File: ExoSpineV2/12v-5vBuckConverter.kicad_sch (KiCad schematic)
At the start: 14 parts, among them J19 Screw_Terminal_01x02, U5 TPS564247

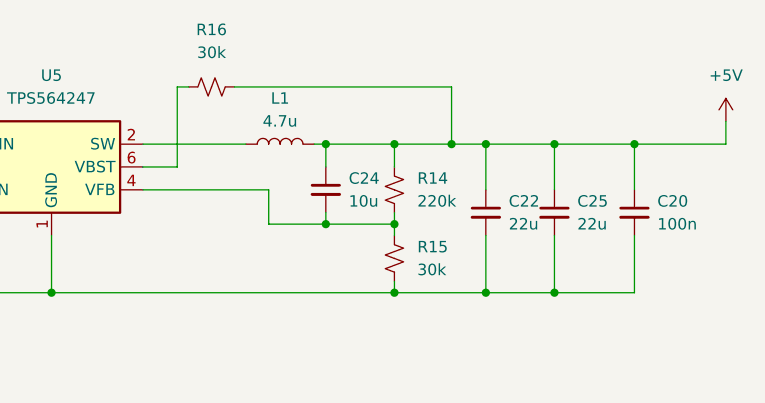
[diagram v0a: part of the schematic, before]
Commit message: dimensionnement des composantes pour le DC-DC
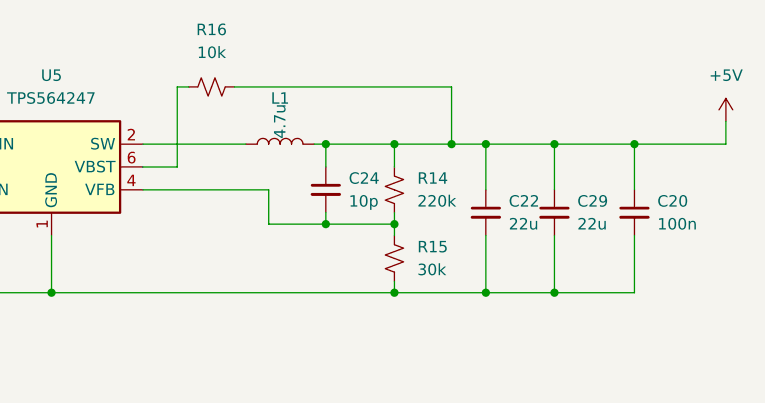
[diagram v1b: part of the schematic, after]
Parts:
- removed C25: 22u, symbol Device:C_Small
- added C29: 22u, Capacitor_SMD:C_0805_2012Metric_Pad1.18x1.45mm_HandSolder, symbol Device:C_Small
- C20, C21, C23: footprint (none) -> Capacitor_SMD:C_1206_3216Metric_Pad1.33x1.80mm_HandSolder
- C22: footprint (none) -> Capacitor_SMD:C_0805_2012Metric_Pad1.18x1.45mm_HandSolder
- C24: value 10u -> 10p; footprint (none) -> Capacitor_SMD:C_0201_0603Metric_Pad0.64x0.40mm_HandSolder
- L1: footprint (none) -> Inductor_SMD:L_Bourns_SRP7028A_7.3x6.6mm
- R12, R13, R14, R15: footprint (none) -> Resistor_SMD:R_0805_2012Metric_Pad1.20x1.40mm_HandSolder
- R16: value 30k -> 10k; footprint (none) -> Resistor_SMD:R_0805_2012Metric_Pad1.20x1.40mm_HandSolder
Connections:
- net +5V: now also R16.1, C29.1; no longer R16.2
- net GND: now also R15.1, C29.2; no longer R15.2
- net at U5.6 (VBST): now also R16.2; no longer R16.1
- net at C24.2, R14.2, U5.4 (VFB): now also R15.2; no longer R15.1

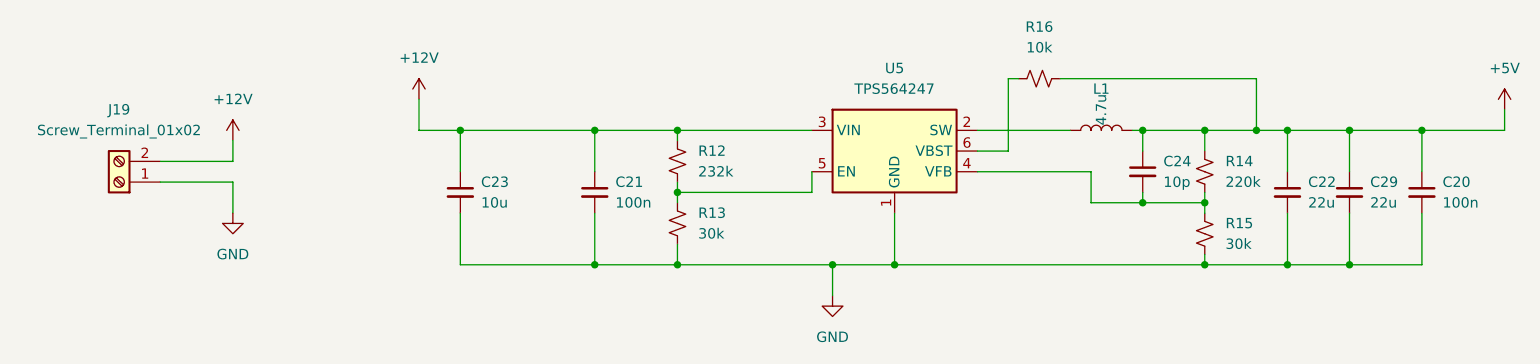
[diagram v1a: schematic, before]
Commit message: ajout de composantes au board
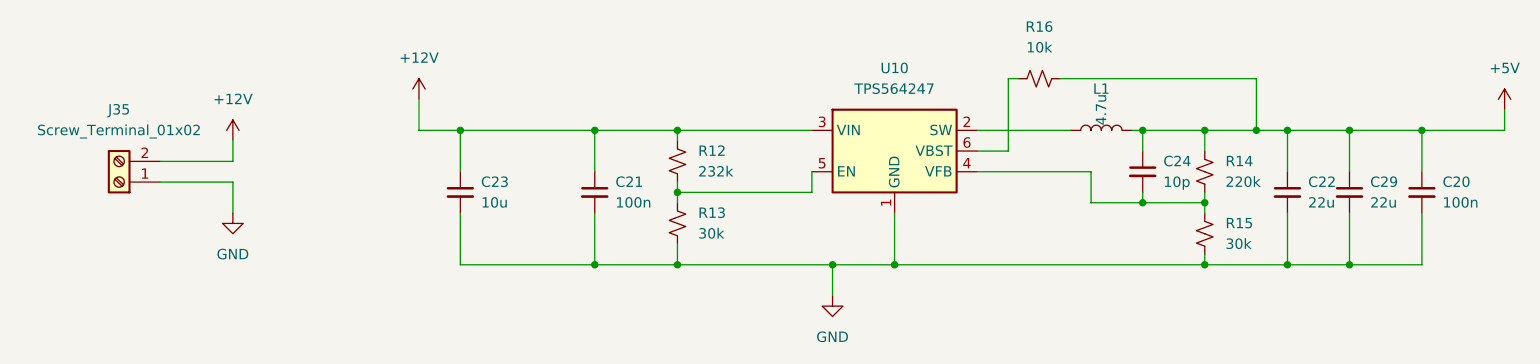
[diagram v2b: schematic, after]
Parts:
- renumbered J19 to J35, U5 to U10
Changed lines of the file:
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@@
   (symbol (lib_id "Connector:Screw_Terminal_01x02") (at 46.99 85.09 180) (unit 1)
     (in_bom yes) (on_board yes) (dnp no) (fields_autoplaced)
-    (property "Reference" "J19" (at 46.99 76.2 0)
+    (property "Reference" "J35" (at 46.99 76.2 0)
       (effects (font (size 1.27 1.27)))
     )
@@
       (project "ExospineV2"
         (path "/e63e39d7-6ac0-4ffd-8aa3-1841a4541b55/9042656c-fbb6-4ad3-be09-ad4e06445cda"
-          (reference "J19") (unit 1)
+          (reference "J35") (unit 1)
         )
       )
@@
   (symbol (lib_id "power:+12V") (at 83.82 74.93 0) (unit 1)
     (in_bom yes) (on_board yes) (dnp no) (fields_autoplaced)
-    (property "Reference" "#PWR011" (at 83.82 78.74 0)
+    (property "Reference" "#PWR0101" (at 83.82 78.74 0)
       (effects (font (size 1.27 1.27)) hide)
     )
@@
       (project "ExospineV2"
         (path "/e63e39d7-6ac0-4ffd-8aa3-1841a4541b55/9042656c-fbb6-4ad3-be09-ad4e06445cda"
-          (reference "#PWR011") (unit 1)
+          (reference "#PWR0101") (unit 1)
         )
       )
@@
   (symbol (lib_id "Regulator_Switching:TPS563200") (at 142.24 81.28 0) (unit 1)
     (in_bom yes) (on_board yes) (dnp no) (fields_autoplaced)
-    (property "Reference" "U5" (at 142.24 71.12 0)
+    (property "Reference" "U10" (at 142.24 71.12 0)
       (effects (font (size 1.27 1.27)))
     )
@@
       (project "ExospineV2"
         (path "/e63e39d7-6ac0-4ffd-8aa3-1841a4541b55/9042656c-fbb6-4ad3-be09-ad4e06445cda"
-          (reference "U5") (unit 1)
+          (reference "U10") (unit 1)
         )
       )
@@
   (symbol (lib_id "power:+5V") (at 217.17 76.2 0) (unit 1)
     (in_bom yes) (on_board yes) (dnp no) (fields_autoplaced)
-    (property "Reference" "#PWR013" (at 217.17 80.01 0)
+    (property "Reference" "#PWR0103" (at 217.17 80.01 0)
       (effects (font (size 1.27 1.27)) hide)
     )
@@
       (project "ExospineV2"
         (path "/e63e39d7-6ac0-4ffd-8aa3-1841a4541b55/9042656c-fbb6-4ad3-be09-ad4e06445cda"
-          (reference "#PWR013") (unit 1)
+          (reference "#PWR0103") (unit 1)
         )
       )
@@
   (symbol (lib_id "power:GND") (at 134.62 99.06 0) (unit 1)
     (in_bom yes) (on_board yes) (dnp no) (fields_autoplaced)
-    (property "Reference" "#PWR014" (at 134.62 105.41 0)
+    (property "Reference" "#PWR0102" (at 134.62 105.41 0)
       (effects (font (size 1.27 1.27)) hide)
     )
@@
       (project "ExospineV2"
         (path "/e63e39d7-6ac0-4ffd-8aa3-1841a4541b55/9042656c-fbb6-4ad3-be09-ad4e06445cda"
-          (reference "#PWR014") (unit 1)
-        )
-      )
+          (reference "#PWR0102") (unit 1)
+        )
+      )

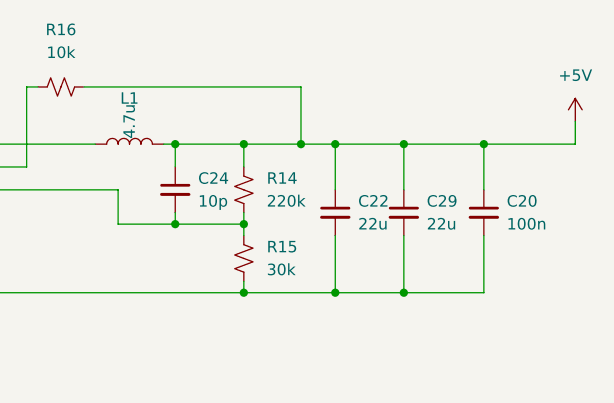
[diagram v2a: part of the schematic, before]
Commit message: dimensionnage de certaines composantes
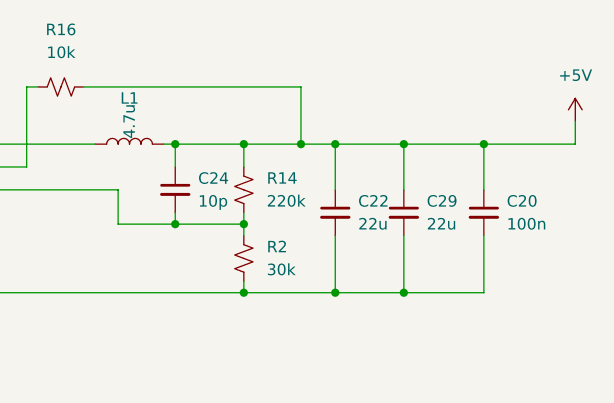
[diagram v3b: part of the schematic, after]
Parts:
- removed R15: 30k, Resistor_SMD:R_0805_2012Metric_Pad1.20x1.40mm_HandSolder, symbol Device:R_Small_US
- added R2: 30k, Resistor_SMD:R_0805_2012Metric_Pad1.20x1.40mm_HandSolder, symbol Device:R_Small_US
- R13: JLCPCB (none) -> https://jlcpcb.com/partdetail/18309-0805W8F3002T5E/C17621
- R14: JLCPCB (none) -> https://jlcpcb.com/partdetail/18244-0805W8F2203T5E/C17556
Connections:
- net GND: now also R2.2
- net at C24.2, R14.2, U10.4 (VFB): now also R2.1
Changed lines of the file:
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@@
     (stroke (width 0) (type default))
   )
-  (wire (pts (xy 217.17 78.74) (xy 217.17 76.2))
+  (wire (pts (xy 217.17 76.2) (xy 217.17 78.74))
     (stroke (width 0) (type default))
   )
@@
       (effects (font (size 1.27 1.27)) hide)
     )
+    (property "JLCPCB" "https://jlcpcb.com/partdetail/18244-0805W8F2203T5E/C17556" (at 180.34 83.82 0)
+      (effects (font (size 1.27 1.27)) hide)
+    )
     (pin "1")
     (pin "2")
@@
     )
   )
+  (symbol (lib_id "Device:R_Small_US") (at 180.34 91.44 0) (unit 1)
+    (in_bom yes) (on_board yes) (dnp no) (fields_autoplaced)
+    (property "Reference" "R2" (at 182.88 90.17 0)
+      (effects (font (size 1.27 1.27)) (justify left))
+    )
+    (property "Value" "30k" (at 182.88 92.71 0)
+      (effects (font (size 1.27 1.27)) (justify left))
+    )
+    (property "Footprint" "Resistor_SMD:R_0805_2012Metric_Pad1.20x1.40mm_HandSolder" (at 180.34 91.44 0)
+      (effects (font (size 1.27 1.27)) hide)
+    )
+    (property "Datasheet" "https://wmsc.lcsc.com/wmsc/upload/file/pdf/v2/lcsc/2205311830_UNI-ROYAL-Uniroyal-Elec-0805W8F3002T5E_C17621.pdf" (at 180.34 91.44 0)
+      (effects (font (size 1.27 1.27)) hide)
+    )
+    (property "JLCPCB" "https://jlcpcb.com/partdetail/18309-0805W8F3002T5E/C17621" (at 180.34 91.44 0)
+      (effects (font (size 1.27 1.27)) hide)
+    )
+    (pin "1")
+    (pin "2")
+    (instances
+      (project "ExospineV2"
+        (path "/e63e39d7-6ac0-4ffd-8aa3-1841a4541b55/9042656c-fbb6-4ad3-be09-ad4e06445cda"
+          (reference "R2") (unit 1)
+        )
+      )
+    )
+  )
   (symbol (lib_id "Device:C_Small") (at 198.12 86.36 0) (unit 1)
     (in_bom yes) (on_board yes) (dnp no) (fields_autoplaced)
@@
       (effects (font (size 1.27 1.27)) hide)
     )
-    (property "Datasheet" "https://wmsc.lcsc.com/wmsc/upload/file/pdf/v2/lcsc/2304140030_FH--Guangdong-Fenghua-Advanced-Tech-TD05H3002DT_C343950.pdf" (at 115.57 90.17 0)
+    (property "Datasheet" "https://wmsc.lcsc.com/wmsc/upload/file/pdf/v2/lcsc/2205311830_UNI-ROYAL-Uniroyal-Elec-0805W8F3002T5E_C17621.pdf" (at 115.57 90.17 0)
+      (effects (font (size 1.27 1.27)) hide)
+    )
+    (property "JLCPCB" "https://jlcpcb.com/partdetail/18309-0805W8F3002T5E/C17621" (at 115.57 90.17 0)
       (effects (font (size 1.27 1.27)) hide)
     )
@@
         )
       )
-    )
-  )
-  (symbol (lib_id "Device:R_Small_US") (at 180.34 91.44 180) (unit 1)
-    (in_bom yes) (on_board yes) (dnp no) (fields_autoplaced)
-    (property "Reference" "R15" (at 182.88 90.17 0)
-      (effects (font (size 1.27 1.27)) (justify right))
-    )
-    (property "Value" "30k" (at 182.88 92.71 0)
-      (effects (font (size 1.27 1.27)) (justify right))
-    )
-    (property "Footprint" "Resistor_SMD:R_0805_2012Metric_Pad1.20x1.40mm_HandSolder" (at 180.34 91.44 0)
-      (effects (font (size 1.27 1.27)) hide)
-    )
-    (property "Datasheet" "https://wmsc.lcsc.com/wmsc/upload/file/pdf/v2/lcsc/2304140030_FH--Guangdong-Fenghua-Advanced-Tech-TD05H3002DT_C343950.pdf" (at 180.34 91.44 0)
-      (effects (font (size 1.27 1.27)) hide)
-    )
-    (pin "1")
-    (pin "2")
-    (instances
-      (project "ExospineV2"
-        (path "/e63e39d7-6ac0-4ffd-8aa3-1841a4541b55/9042656c-fbb6-4ad3-be09-ad4e06445cda"
-          (reference "R15") (unit 1)
-        )
-      )

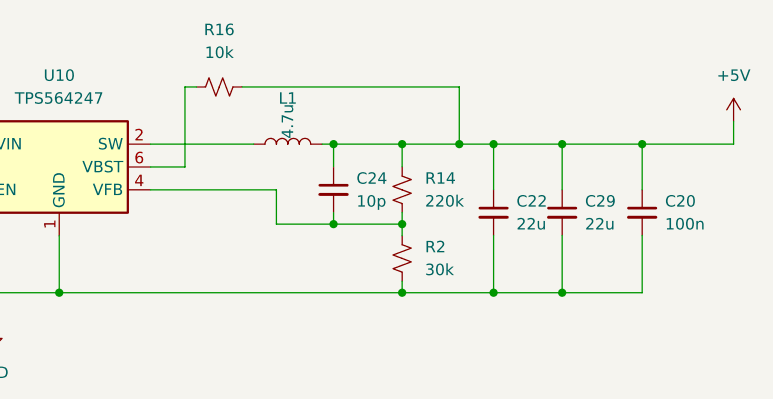
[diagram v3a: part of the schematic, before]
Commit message: changement de un peu de librairies de parts, finition du premier PCB
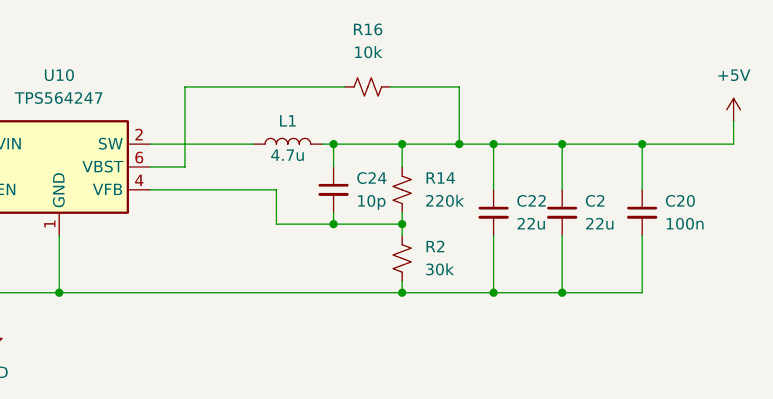
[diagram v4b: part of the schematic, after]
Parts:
- removed C29: 22u, Capacitor_SMD:C_0805_2012Metric_Pad1.18x1.45mm_HandSolder, symbol Device:C_Small
- added C2: 22u, Capacitor_SMD:C_0805_2012Metric_Pad1.18x1.45mm_HandSolder, symbol Device:C_Small
- C20, C21: JLCPCB (none) -> https://jlcpcb.com/partdetail/25237-CL31B104KBCNNNC/C24497
- C22: Field4 (none) -> https://jlcpcb.com/partdetail/46786-CL21A226MAQNNNE/C45783
- C23: JLCPCB (none) -> https://jlcpcb.com/partdetail/14236-CL31A106KBHNNNE/C13585
- C24: JLCPCB (none) -> https://jlcpcb.com/partdetail/1986-CL10C100JB8NNNC/C1634
- R16: JLCPCB (none) -> https://passport.jlcpcb.com/#/login?response_type=code&clie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
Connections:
- net +5V: now also C2.1
- net GND: now also C2.2
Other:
- moved on the sheet: R16
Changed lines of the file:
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@@
     (stroke (width 0) (type default))
   )
-  (wire (pts (xy 156.21 72.39) (xy 157.48 72.39))
+  (wire (pts (xy 156.21 72.39) (xy 173.99 72.39))
     (stroke (width 0) (type default))
   )
@@
     (stroke (width 0) (type default))
   )
-  (wire (pts (xy 162.56 72.39) (xy 186.69 72.39))
+  (wire (pts (xy 179.07 72.39) (xy 186.69 72.39))
     (stroke (width 0) (type default))
   )
@@
       (effects (font (size 1.27 1.27)) hide)
     )
-    (property "Datasheet" "https://wmsc.lcsc.com/wmsc/upload/file/pdf/v2/lcsc/2208181800_FOJAN-FCC0805X226M100FT_C5137600.pdf" (at 190.5 86.36 0)
+    (property "Datasheet" "https://wmsc.lcsc.com/wmsc/upload/file/pdf/v2/lcsc/2304140030_Samsung-Electro-Mechanics-CL21A226MAQNNNE_C45783.pdf" (at 190.5 86.36 0)
+      (effects (font (size 1.27 1.27)) hide)
+    )
+    (property "Field4" "https://jlcpcb.com/partdetail/46786-CL21A226MAQNNNE/C45783" (at 190.5 86.36 0)
       (effects (font (size 1.27 1.27)) hide)
     )
@@
       (effects (font (size 1.27 1.27)) hide)
     )
-    (property "Datasheet" "https://wmsc.lcsc.com/wmsc/upload/file/pdf/v2/lcsc/2208181800_FOJAN-FCC1206B104K500DT_C5137631.pdf" (at 207.01 86.36 0)
+    (property "Datasheet" "https://wmsc.lcsc.com/wmsc/upload/file/pdf/v2/lcsc/2304140030_Samsung-Electro-Mechanics-CL31B104KBCNNNC_C24497.pdf" (at 207.01 86.36 0)
+      (effects (font (size 1.27 1.27)) hide)
+    )
+    (property "JLCPCB" "https://jlcpcb.com/partdetail/25237-CL31B104KBCNNNC/C24497" (at 207.01 86.36 0)
       (effects (font (size 1.27 1.27)) hide)
     )
@@
         (path "/e63e39d7-6ac0-4ffd-8aa3-1841a4541b55/9042656c-fbb6-4ad3-be09-ad4e06445cda"
           (reference "C20") (unit 1)
+        )
+      )
+    )
+  )
+  (symbol (lib_id "Device:C_Small") (at 198.12 86.36 0) (unit 1)
+    (in_bom yes) (on_board yes) (dnp no) (fields_autoplaced)
+    (property "Reference" "C2" (at 200.66 85.0963 0)
+      (effects (font (size 1.27 1.27)) (justify left))
+    )
+    (property "Value" "22u" (at 200.66 87.6363 0)
+      (effects (font (size 1.27 1.27)) (justify left))
+    )
+    (property "Footprint" "Capacitor_SMD:C_0805_2012Metric_Pad1.18x1.45mm_HandSolder" (at 198.12 86.36 0)
+      (effects (font (size 1.27 1.27)) hide)
+    )
+    (property "Datasheet" "https://wmsc.lcsc.com/wmsc/upload/file/pdf/v2/lcsc/2304140030_Samsung-Electro-Mechanics-CL21A226MAQNNNE_C45783.pdf" (at 198.12 86.36 0)
+      (effects (font (size 1.27 1.27)) hide)
+    )
+    (property "Field4" "https://jlcpcb.com/partdetail/46786-CL21A226MAQNNNE/C45783" (at 198.12 86.36 0)
+      (effects (font (size 1.27 1.27)) hide)
+    )
+    (pin "1")
+    (pin "2")
+    (instances
+      (project "ExospineV2"
+        (path "/e63e39d7-6ac0-4ffd-8aa3-1841a4541b55/9042656c-fbb6-4ad3-be09-ad4e06445cda"
+          (reference "C2") (unit 1)
         )
       )
@@
       (effects (font (size 1.27 1.27)) hide)
     )
-    (property "Datasheet" "https://wmsc.lcsc.com/wmsc/upload/file/pdf/v2/lcsc/2208181800_FOJAN-FCC1206B104K500DT_C5137631.pdf" (at 105.41 86.36 0)
+    (property "Datasheet" "https://wmsc.lcsc.com/wmsc/upload/file/pdf/v2/lcsc/2304140030_Samsung-Electro-Mechanics-CL31B104KBCNNNC_C24497.pdf" (at 105.41 86.36 0)
+      (effects (font (size 1.27 1.27)) hide)
+    )
+    (property "JLCPCB" "https://jlcpcb.com/partdetail/25237-CL31B104KBCNNNC/C24497" (at 105.41 86.36 0)
       (effects (font (size 1.27 1.27)) hide)
     )
@@
     )
   )
-  (symbol (lib_id "Device:R_Small_US") (at 160.02 72.39 270) (unit 1)
-    (in_bom yes) (on_board yes) (dnp no) (fields_autoplaced)
-    (property "Reference" "R16" (at 160.02 66.04 90)
-      (effects (font (size 1.27 1.27)))
-    )
-    (property "Value" "10k" (at 160.02 68.58 90)
-      (effects (font (size 1.27 1.27)))
-    )
-    (property "Footprint" "Resistor_SMD:R_0805_2012Metric_Pad1.20x1.40mm_HandSolder" (at 160.02 72.39 0)
-      (effects (font (size 1.27 1.27)) hide)
-    )
-    (property "Datasheet" "https://wmsc.lcsc.com/wmsc/upload/file/pdf/v2/lcsc/2304140030_FH--Guangdong-Fenghua-Advanced-Tech-TD05H3002DT_C343950.pdf" (at 160.02 72.39 0)
+  (symbol (lib_id "Device:R_Small_US") (at 176.53 72.39 270) (unit 1)
+    (in_bom yes) (on_board yes) (dnp no) (fields_autoplaced)
+    (property "Reference" "R16" (at 176.53 66.04 90)
+      (effects (font (size 1.27 1.27)))
+    )
+    (property "Value" "10k" (at 176.53 68.58 90)
+      (effects (font (size 1.27 1.27)))
+    )
+    (property "Footprint" "Resistor_SMD:R_0805_2012Metric_Pad1.20x1.40mm_HandSolder" (at 176.53 72.39 0)
+      (effects (font (size 1.27 1.27)) hide)
+    )
+    (property "Datasheet" "https://wmsc.lcsc.com/wmsc/upload/file/pdf/v2/lcsc/2206010216_UNI-ROYAL-Uniroyal-Elec-0805W8F1002T5E_C17414.pdf" (at 176.53 72.39 0) (show_name)
+      (effects (font (size 1.27 1.27)) hide)
+    )
+    (property "JLCPCB" "https://passport.jlcpcb.com/#/login?response_type=code&client_id=34495309ae47483ebf71827b5bcb591c&redirect_url=https%3A%2F%2Fjlcpcb.com%2Fauth%2Flogin%3Furl%3Dhttps%253A%252F%252Fjlcpcb.com%252Fparts%252F1st%252FResistors_2%2526_t%3D1712330818399&state=RDPqofFaHWeXoV4oRNQJkmP28Dy7Dc1pSmrNnbR2%2BoJti%2FunKuARpm6vK7vks6gvxXlxT2jRqDC2pDnubS09JjYXyZCHCy3YC1j%2B9wzOsFE3k0nUifNqqd055Dfdv79jXq6hiPRPdIXIxZSHfBen8EQSijPoY3AV%2FSU0WsTEH%2F2OkXM1o2nCvyMXc1jvAJ3rsivBKx%2Fq77G7xXOi04%2B%2BWQ%3D%3D&from=jlcpcb" (at 176.53 72.39 90)
       (effects (font (size 1.27 1.27)) hide)
     )
@@
       (effects (font (size 1.27 1.27)) hide)
     )
-    (property "Datasheet" "https://wmsc.lcsc.com/wmsc/upload/file/pdf/v2/lcsc/1810171714_Taiyo-Yuden-TMK316BJ106ML-T_C311699.pdf" (at 88.9 86.36 0)
+    (property "Datasheet" "https://wmsc.lcsc.com/wmsc/upload/file/pdf/v2/lcsc/2304140030_Samsung-Electro-Mechanics-CL31A106KBHNNNE_C13585.pdf" (at 88.9 86.36 0)
+      (effects (font (size 1.27 1.27)) hide)
+    )
+    (property "JLCPCB" "https://jlcpcb.com/partdetail/14236-CL31A106KBHNNNE/C13585" (at 88.9 86.36 0)
       (effects (font (size 1.27 1.27)) hide)
     )
@@
       (effects (font (size 1.27 1.27)) hide)
     )
-    (property "Datasheet" "https://wmsc.lcsc.com/wmsc/upload/file/pdf/v2/lcsc/1808291131_Guangdong-TOPAZ-Elec-Tech-0603B104K500CT_C167026.pdf" (at 172.72 83.82 0)
+    (property "Datasheet" "https://wmsc.lcsc.com/wmsc/upload/file/pdf/v2/lcsc/2304140030_Samsung-Electro-Mechanics-CL10C100JB8NNNC_C1634.pdf" (at 172.72 83.82 0)
+      (effects (font (size 1.27 1.27)) hide)
+    )
+    (property "JLCPCB" "https://jlcpcb.com/partdetail/1986-CL10C100JB8NNNC/C1634" (at 172.72 83.82 0)
       (effects (font (size 1.27 1.27)) hide)
     )
@@
   (symbol (lib_id "Device:L") (at 167.64 78.74 90) (unit 1)
     (in_bom yes) (on_board yes) (dnp no)
-    (property "Reference" "L1" (at 167.64 73.66 90)
-      (effects (font (size 1.27 1.27)))
-    )
-    (property "Value" "4.7u" (at 167.64 76.2 0)
+    (property "Reference" "L1" (at 167.64 76.2 90)
+      (effects (font (size 1.27 1.27)))
+    )
+    (property "Value" "4.7u" (at 167.64 80.01 90)
       (effects (font (size 1.27 1.27)))
     )
@@
         )
       )
-    )
-  )
-  (symbol (lib_id "Device:C_Small") (at 198.12 86.36 0) (unit 1)
-    (in_bom yes) (on_board yes) (dnp no) (fields_autoplaced)
-    (property "Reference" "C29" (at 200.66 85.0963 0)
-      (effects (font (size 1.27 1.27)) (justify left))
-    )
-    (property "Value" "22u" (at 200.66 87.6363 0)
-      (effects (font (size 1.27 1.27)) (justify left))
-    )
-    (property "Footprint" "Capacitor_SMD:C_0805_2012Metric_Pad1.18x1.45mm_HandSolder" (at 198.12 86.36 0)
-      (effects (font (size 1.27 1.27)) hide)
-    )
-    (property "Datasheet" "https://wmsc.lcsc.com/wmsc/upload/file/pdf/v2/lcsc/2208181800_FOJAN-FCC0805X226M100FT_C5137600.pdf" (at 198.12 86.36 0)
-      (effects (font (size 1.27 1.27)) hide)
-    )
-    (pin "1")
-    (pin "2")
-    (instances
-      (project "ExospineV2"
-        (path "/e63e39d7-6ac0-4ffd-8aa3-1841a4541b55/9042656c-fbb6-4ad3-be09-ad4e06445cda"
-          (reference "C29") (unit 1)
-        )
-      )
